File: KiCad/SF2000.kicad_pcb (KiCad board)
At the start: 4 copper layers, 111.5 x 83.9 mm, 105 parts, among them J1 Conn_2Rows-86Pins_even_odd, J10 Conn_02x01, J11 Conn_02x01, J2 Conn_01x02, J20 Conn_02x11_Odd_Even, J3 Conn_02x05_Odd_Even, J4 Conn_02x01, J5 Conn_01x01, J6 Micro_SD_Card_Socket, J7 Conn_02x01, J8 Conn_02x01, J9 Conn_02x01, Q1 MMBT3904, Q2 MMBT3906, U1 LM1117-3.3, U10 IS61WV20488FBLL-10TLI, U11 IS61WV20488FBLL-10TLI, U12 IS61WV20488FBLL-10TLI, U13 IS61WV20488FBLL-10TLI, U14 SST39LF040, U15 SST39LF802C, U16 74AHCT3G14, U2 ABLIC S-1132B43-M5T1U, U20 AT25SF081B-SSH, U3 TLV74312PDBV, U4 SN74CBT16211, U5 SN74CBT16211, U6 SN74CBT16211, U7 SN74AUP1T87DCKR, U8 T8Q144C3, U9 68000D, X1 Oscillator_7.0x5.0mm

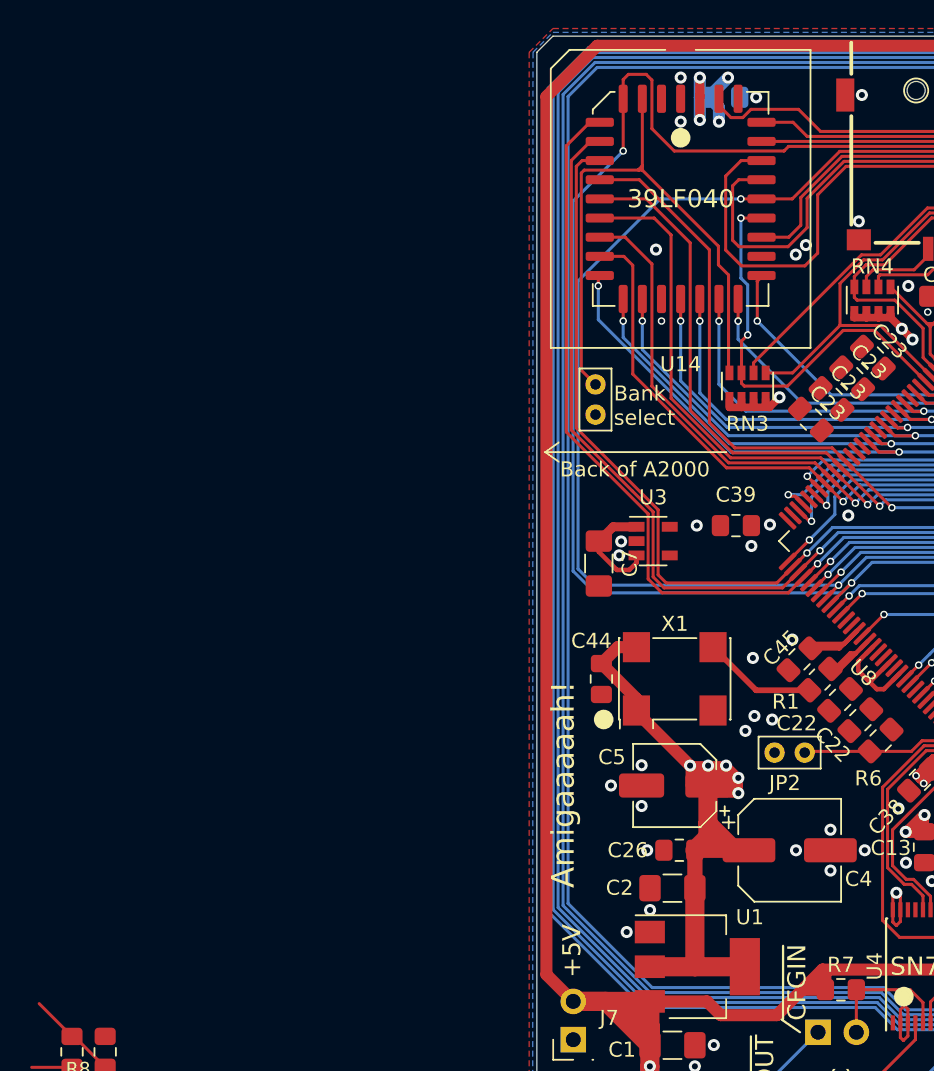
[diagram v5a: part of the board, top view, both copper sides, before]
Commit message: Add caps for 1.2V voltage regulator and place and route the area
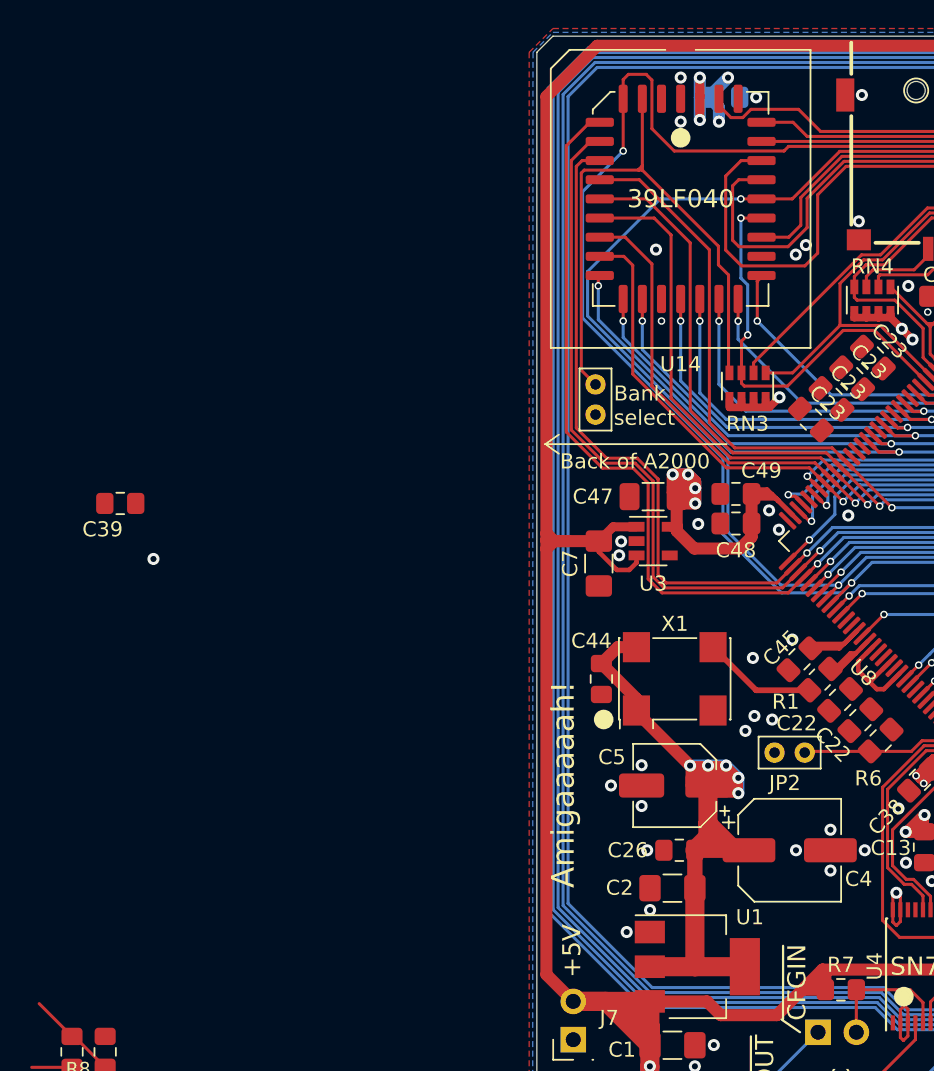
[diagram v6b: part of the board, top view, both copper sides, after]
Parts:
- added C47: 10uF, Capacitor_SMD:C_1206_3216Metric_Pad1.33x1.80mm_HandSolder, F.Cu at (105.4, 89.6)
- added C48: 0.1uF, Capacitor_SMD:C_0805_2012Metric_Pad1.18x1.45mm_HandSolder, F.Cu at (110.9, 91.4)
- added C49: 0.01uF, Capacitor_SMD:C_0805_2012Metric_Pad1.18x1.45mm_HandSolder, F.Cu at (110.9, 89.5)
- moved C39 40.8 mm to (70.0, 90.1)
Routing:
- net 1V2: track 50.1 -> 84.7 mm, vias 6 -> 10
- net A12_3V3: track 235.2 -> 227.4 mm
- net A13_3V3: track 251.0 -> 243.2 mm
- net +5VDC: track 263.9 -> 269.8 mm
- net 3V3: track 289.1 -> 293.7 mm
- net A6_3V3: track 211.2 -> 212.4 mm
- net A8_3V3: track 217.5 -> 218.7 mm
- net A7_3V3: track 213.9 -> 215.1 mm
- net GND: vias 118 -> 119

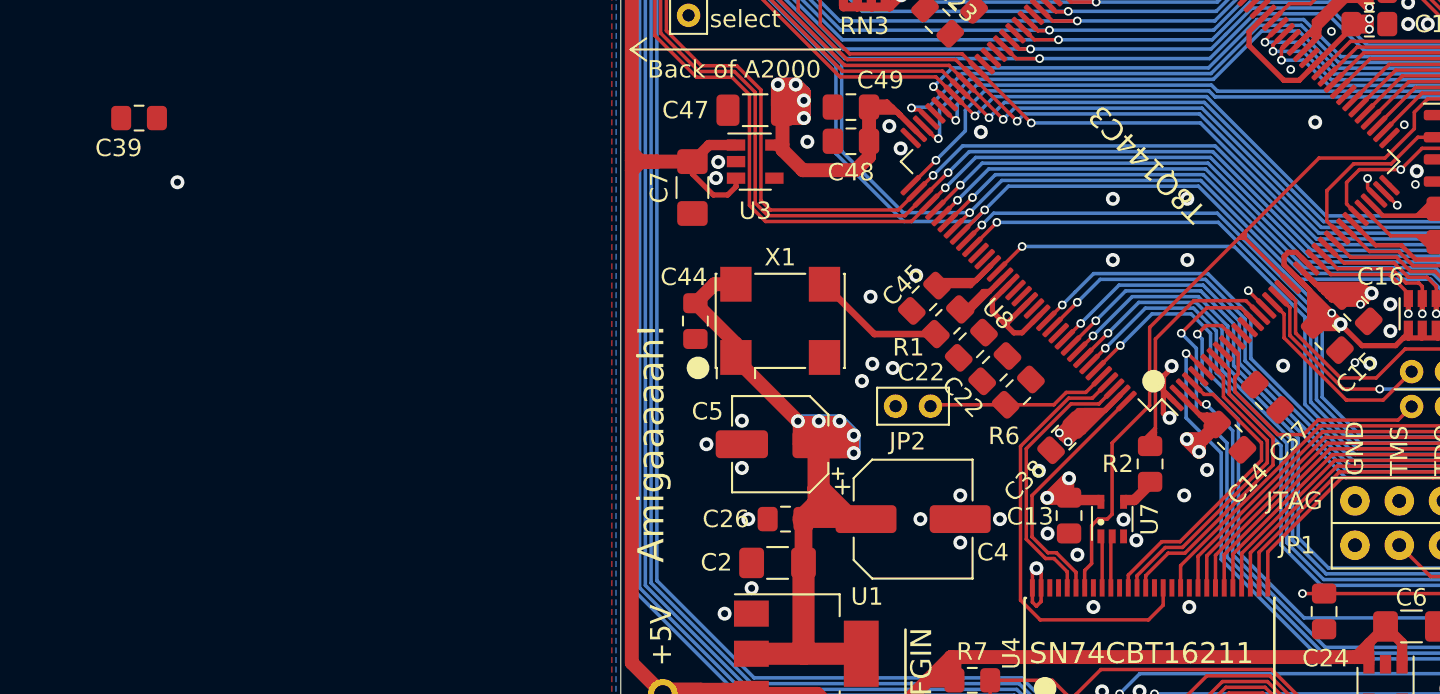
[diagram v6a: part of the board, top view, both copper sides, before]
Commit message: Placement of C39
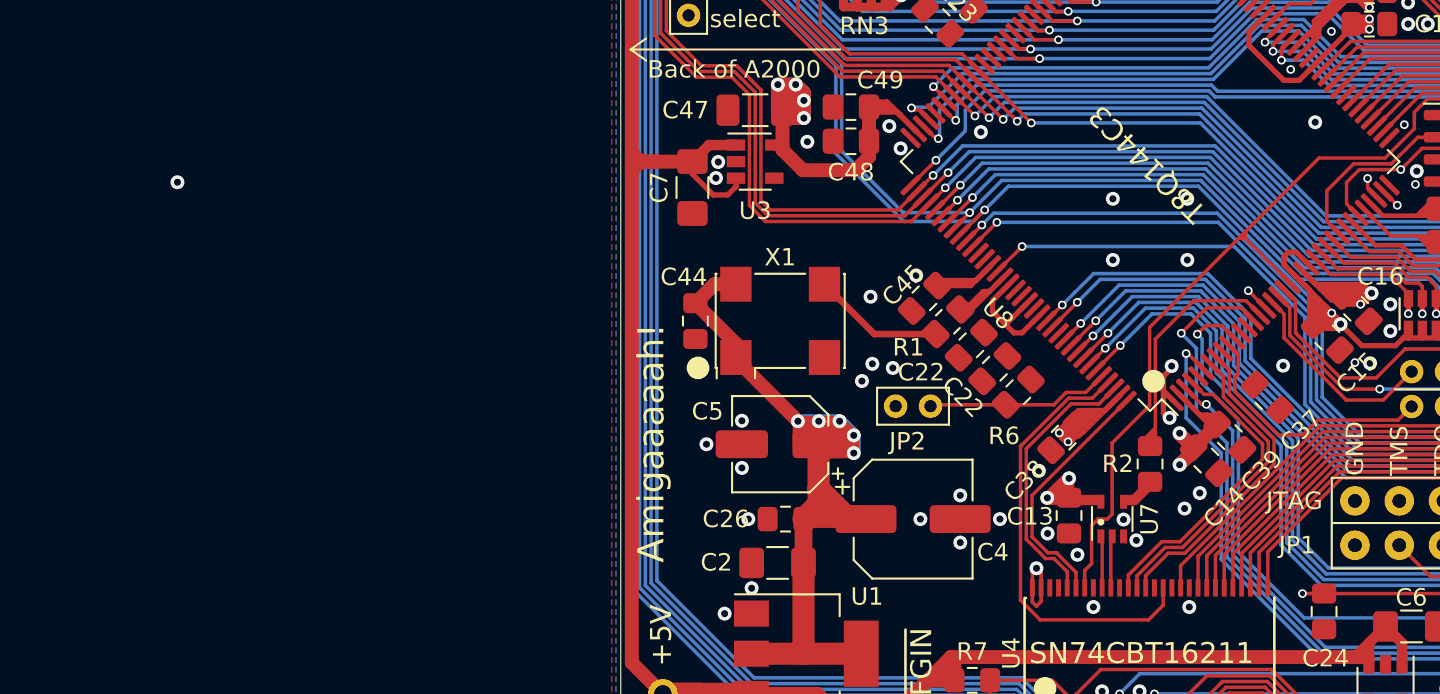
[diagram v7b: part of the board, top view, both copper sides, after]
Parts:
- moved C39 65.2 mm to (132.6, 108.4), turned to 135 degrees
- moved C14 1.90 mm to (131.2, 109.7)
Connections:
- C39 pad 2: 3V3 -> 1V2
